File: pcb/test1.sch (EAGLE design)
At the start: 6 parts, among them IC1 FT232RL, IC2 ACS758ECB-200B-PFF-T, U1 STM32F10XRXT6, X1 FPS009-30003

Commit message: skematik dulu
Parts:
- removed X1: FPS009-30003, con-yamaichi:FPS009-30003
- added BOOT: (no value), pinhead:PINHD-1X3
- added C-33VA, C-5VA, C-PWR1: 1000uf/25v, resistor:CPOL-EU153CLV-1014
- added C-33VB, C-5VB, C-OSCA, C-OSCA1, C-OSCB, C-OSCB1, C-PWR2: 22pf, resistor:C-EUC1206
- added C-I0, C-I1, C-V0, C-V1: 100nf, resistor:C-EUC1206
- added D1: (no value), diode:DIODE-SMC
- added D2: 3v6, diode:ZENER-DIODESMB
- added DIS1: TUXGR_16X2_R2, display-lcd:TUXGR_16X2_R2
- added IC3: ACS758ECB-200B-PFF-T, allegro:ACS758ECB-200B-PFF-T
- added IC4: 7805TV, linear:7805TV
- added IC5: LM1117, v-reg:LM317TL
- added J1: (no value), sd-mmc:SDCARD
- added L-PWR, L-RUN: (no value), led:LEDSML1206
- added PAD-PWR+, PAD-PWR-, PAD-V0, PAD-V1: (no value), wirepad:3,81/1,4
- added PAD33-12, PAD33-5, PAD33-IN: WIREPADSMD2,54-5,08, wirepad:WIREPADSMD2,54-5,08
- added Q1: 8mhz, crystal:CRYSTALHC49S
- added Q2: 32khz, crystal:CRYSTALTC26V
- added R-33A: 270, resistor:R-EU_R1206
- added R-33B, R-PWR, R-RUN: 330, resistor:R-EU_R1206
- added R-IA0, R-IA1, R-IB0, R-IB1, R-VA0, R-VA1, R-VB0, R-VB1: 4k7, resistor:R-EU_R1206
- added R-LCD: 560, resistor:R-EU_R1206
- added R-MMC0, R-MMC1, R-MMC2: 10k, resistor:R-EU_R1206
- added USB-VCC: (no value), pinhead:PINHD-1X2
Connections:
- new net N$10: L-RUN.A, R-RUN.1
- new net N$11: C-PWR1.+, C-PWR2.1, D1.A, PAD-PWR+.P
- new net N$12: IC5.IN, PAD33-IN.P
- new net N$13: PAD33-12.P
- new net N$14: PAD33-5.P
- new net N$15: IC5.ADJ, R-33A.1, R-33B.2
- new net N$16: BOOT.2, U1RESET.BOOT0
- new net N$18: J1.DAT1, R-MMC1.2
- new net N$19: J1.DAT2, R-MMC0.2
- new net N$3: IC2.VOUT, R-IA0.1
- new net N$4: IC2.IP+, R-VA0.1
- new net N$5: JP1.VCC, USB-VCC.1
- new net N$6: IC3.VOUT, R-IA1.1
- new net N$7: IC3.IP+, R-VA1.1
- new net N$8: DIS1.CONTR, R-LCD.2
- new net N$9: L-PWR.A, R-PWR.1
- new net V12: D1.C, IC4.VI
- net D4: now also DIS1.D4
- net D5: now also DIS1.D5
- net D6: now also DIS1.D6
- net D7: now also DIS1.D7
- net EN: now also DIS1.E
- net I0: now also C-I0.2, R-IA0.2, R-IB0.2
- net I1: now also C-I1.2, R-IA1.2, R-IB1.2
- net MISO: now also J1.DAT0/DO, R-MMC2.2
- net MOSI: now also J1.CMD/DI
- net NSS: now also J1.CD/DAT3/CS
- net OSC32A: now also C-OSCA1.1, Q2.2
- net OSC32B: now also C-OSCB1.1, Q2.1
- net OSCA: now also C-OSCA.1, Q1.2
- net OSCB: now also C-OSCB.1, Q1.1
- net RS: now also DIS1.RS
- net RUN: now also L-RUN.C
- net RW: now also DIS1.R/W
- net SCK: now also J1.CLK/SCLK
- net V0: now also C-V0.2, R-VA0.2, R-VB0.2
- net V1: now also C-V1.2, R-VA1.2, R-VB1.2
- net VCC: now also C-5VA.+, C-5VB.1, DIS1.NC@1, DIS1.VCC, IC2.VCC, IC3.VCC, IC4.VO, USB-VCC.2; no longer JP1.VCC
- net VDD: now also BOOT.3, C-33VA.+, C-33VB.1, D2.C, IC5.OUT, J1.VDD, R-33A.2, R-MMC0.1, R-MMC1.1, R-MMC2.1, R-PWR.2, R-RUN.2, U1RESET.NRST
- net VSS: now also BOOT.1, C-33VA.-, C-33VB.2, C-5VA.-, C-5VB.2, C-I0.1, C-I1.1, C-OSCA.2, C-OSCA1.2, C-OSCB.2, C-OSCB1.2, C-PWR1.-, C-PWR2.2, C-V0.1, C-V1.1, D2.A, DIS1.GND, DIS1.NC@2, IC2.GND, IC3.GND, IC4.GND, J1.CDI#, J1.GND@1, J1.GND@2, J1.GND@3, J1.GND@4, J1.VSS1, J1.VSS2, J1.WP, L-PWR.C, PAD-PWR-.P, PAD-V0.P, PAD-V1.P, R-33B.1, R-IB0.1, R-IB1.1, R-LCD.1, R-VB0.1, R-VB1.1, U1PORTA_H.PA11, U1PORTA_H.PA12, U1PORTA_H.PA13, U1PORTA_H.PA14, U1PORTA_H.PA15, U1PORTA_L.PA4, U1PORTA_L.PA5, U1PORTA_L.PA6, U1PORTA_L.PA7, U1PORTB_H.PB10, U1PORTB_H.PB11, U1PORTB_H.PB8, U1PORTB_H.PB9, U1PORTB_L.PB0, U1PORTB_L.PB1, U1PORTB_L.PB3, U1PORTC_H.PC13, U1PORTC_H.PC8, U1PORTC_H.PC9, U1PORTC_L.PC0, U1PORTC_L.PC1, U1PORTC_L.PC2, U1PORTC_L.PC3, U1PORTC_L.PC4, U1PORTC_L.PC5, U1PORTC_L.PC6, U1PORTC_L.PC7
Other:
- moved on the sheet: IC2

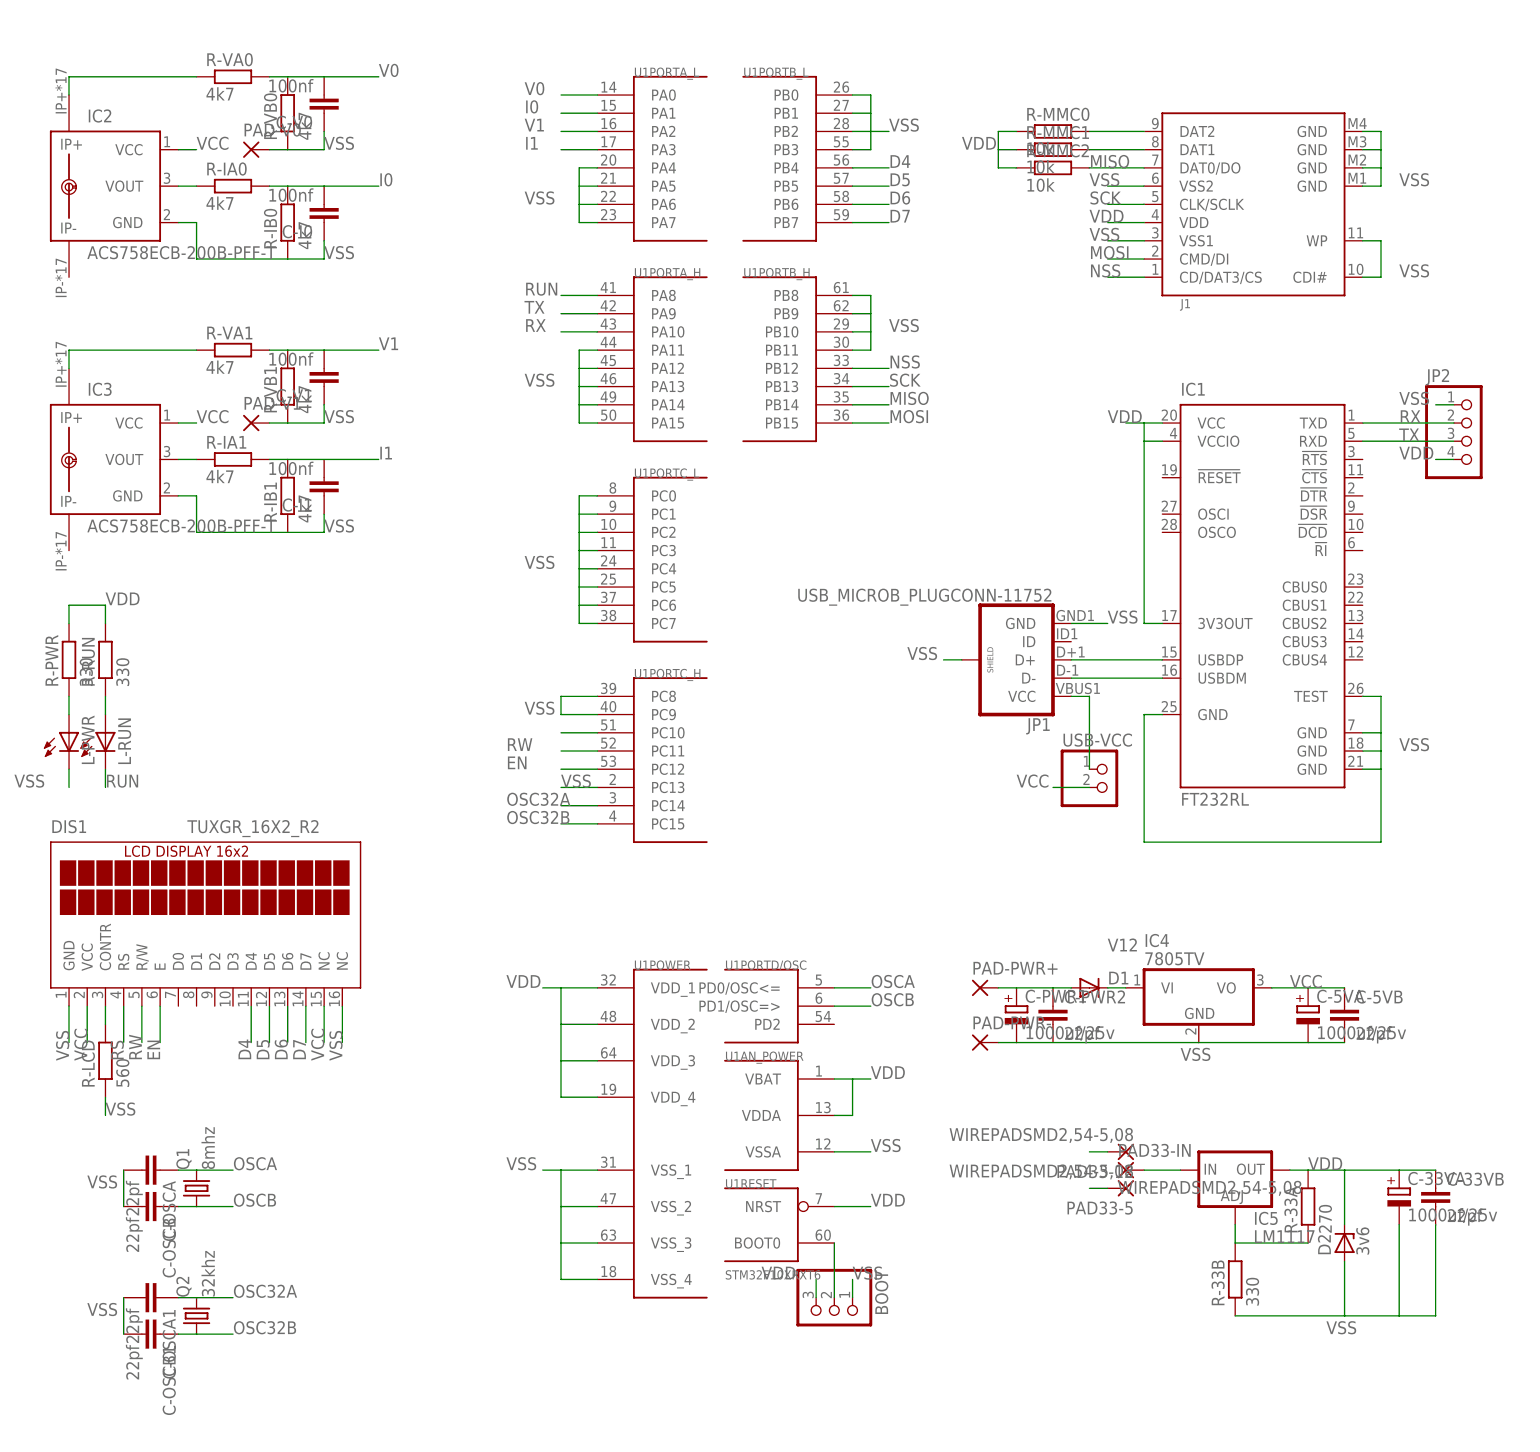
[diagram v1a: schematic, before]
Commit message: ready to manufactured and trial
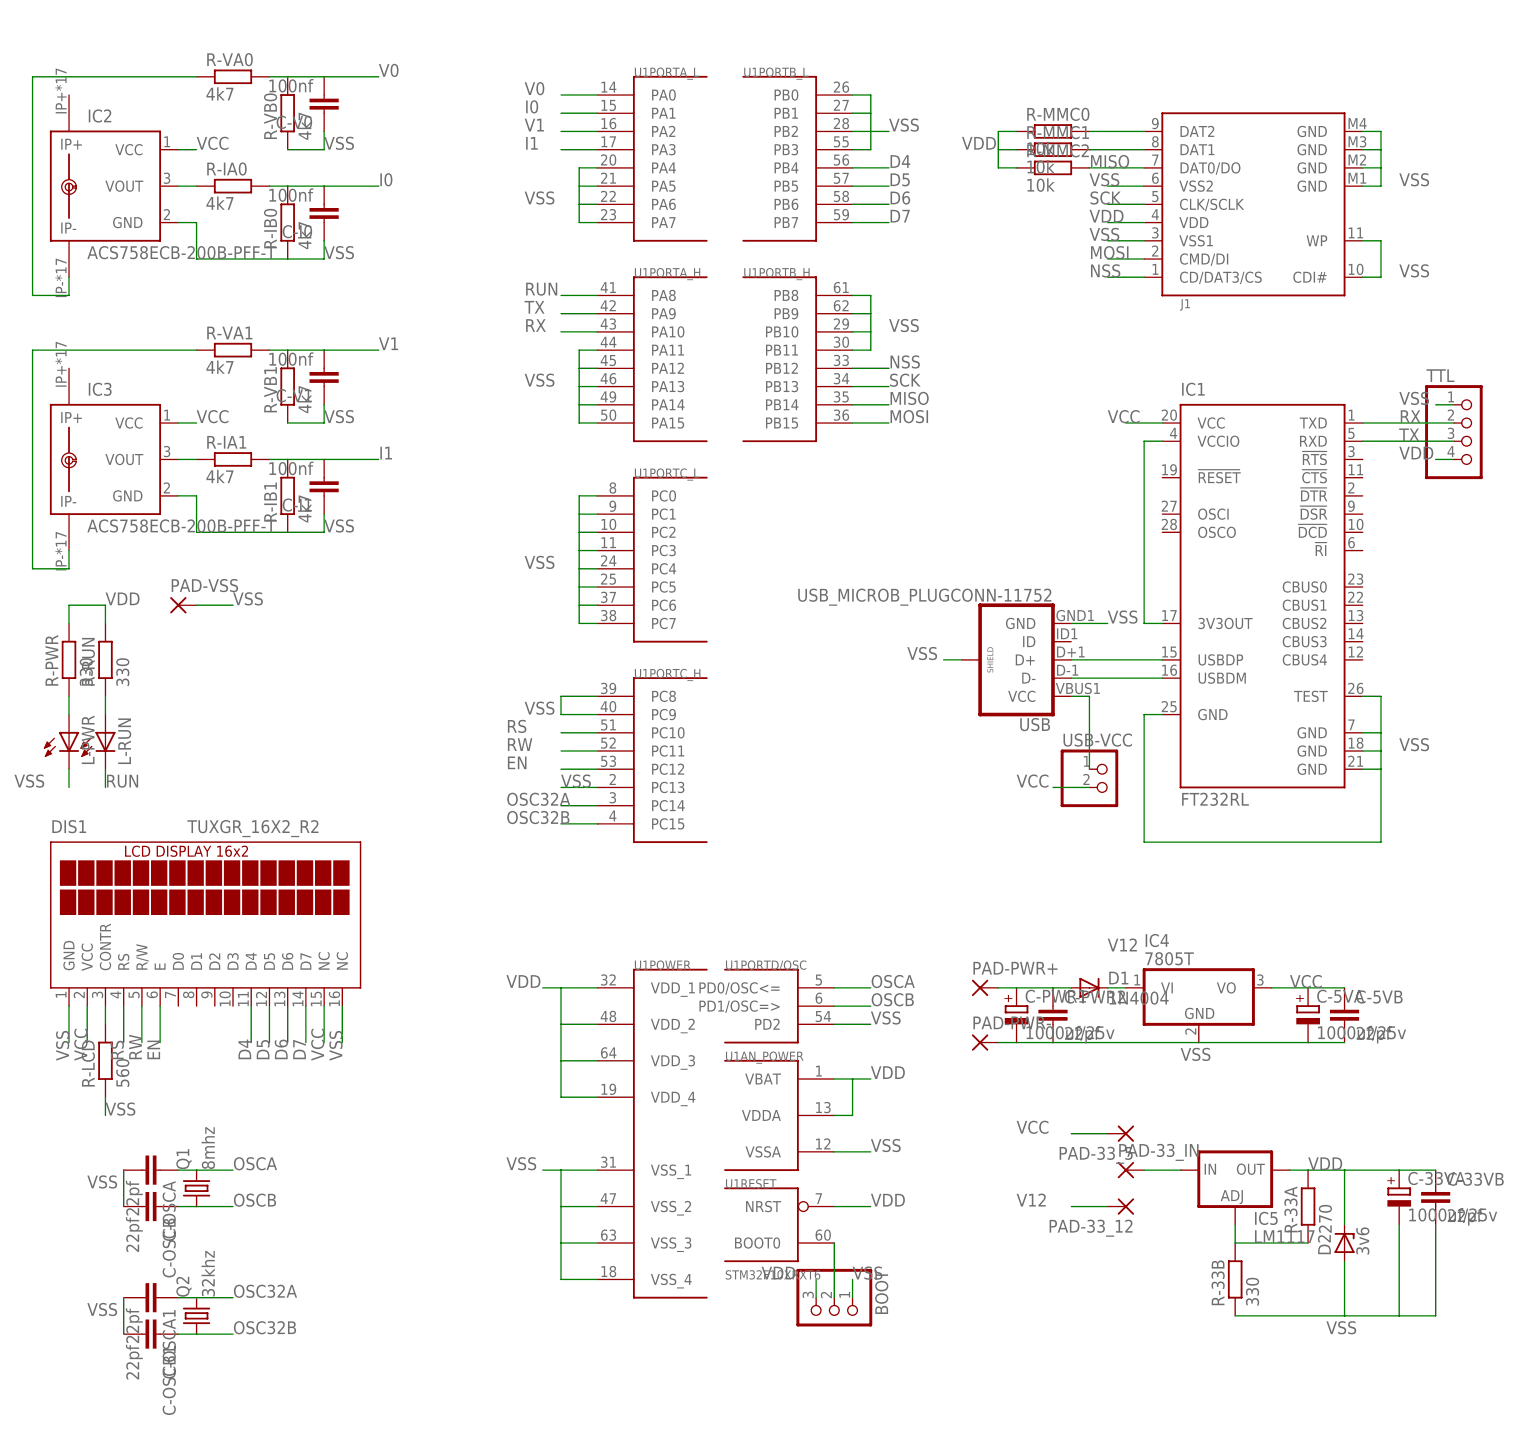
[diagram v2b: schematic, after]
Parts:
- removed PAD-V0, PAD-V1: (no value), wirepad:3,81/1,4
- removed PAD33-12, PAD33-5, PAD33-IN: WIREPADSMD2,54-5,08, wirepad:WIREPADSMD2,54-5,08
- added PAD-33_12, PAD-33_5, PAD-33_IN, PAD-VSS: (no value), wirepad:3,81/1,4
- C-33VA, C-5VA, C-PWR1: device resistor:CPOL-EU153CLV-1014 -> resistor:CPOL-EUE2-5
- D1: value (none) -> 1N4004; device diode:DIODE-SMC -> diode:1N4004
- IC4: value 7805TV -> 7805T; device linear:7805TV -> linear:7805T
- renumbered JP1 to USB, JP2 to TTL
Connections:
- removed net N$13: PAD33-12.P
- removed net N$14: PAD33-5.P
- net N$12: now also PAD-33_IN.P; no longer PAD33-IN.P
- net N$4: now also IC2.IP-; no longer IC2.IP+
- net N$7: now also IC3.IP-; no longer IC3.IP+
- net V12: now also PAD-33_12.P
- net VCC: now also IC1.VCC, PAD-33_5.P
- net VDD: no longer IC1.VCC
- net VSS: now also PAD-VSS.P, U1PORTD/OSC.PD2; no longer PAD-V0.P, PAD-V1.P
